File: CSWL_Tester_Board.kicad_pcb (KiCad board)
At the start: 2 copper layers, 164 parts, among them J1 DB9_Female ID09S33E4GV00LF, J10 Conn_01x03_Male, J11 Conn_01x02, J12 Conn_01x02, J13 Conn_01x02, J14 Conn_01x04, J15 SPI1, J16 Conn_02x10_Odd_Even, J17 Conn_01x02, J18 Conn_01x02, J19 Conn_01x02, J2 Conn_01x04, J20 Conn_01x02, J22 Conn_01x02, J23 Conn_01x03, J24 Conn_01x02, J25 USB_B_Micro, J26 Conn_01x04, J27 Conn_01x10, J3 Conn_01x04, J4 Conn_01x04, J5 DB9_Female ID09S33E4GV00LF, J6 Conn_01x04, J7 Conn_01x04, J8 DB9_Female ID09S33E4GV00LF, J9 Conn_Coaxial_Power, K1 G6SU-2 DC5, K2 G6SU-2 DC5, K3 G6SU-2 DC5, K4 G6SU-2 DC5, K5 G6SU-2 DC5, Q1 DMG2301L, Q10 2N7002LT1G, Q11 2N7002LT1G, Q2 DMG2301L, Q3 DMG2301L, Q4 2N7002LT1G, Q5 2N7002LT1G, Q6 2N7002LT1G, Q7 DMG2301L, Q8 DMG2301L, U1 MAX3221EIPW, U10 EL817-S1-A (NC), U2 STM32F103RCT6, U3 MAX3221EIPW, U4 MCP1700T-3302E_TT, U5 MAX3221EIPW, U6 EL817-S1-A (NC), U7 EL817-S1-A (NC), U8 EL817-S1-A (NC), U9 EL817-S1-A (NC), Y1 8MHz

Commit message: Ruan: pcb developing
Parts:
- removed R62, R68, R70, R71: 0R, Resistor_SMD:R_0603_1608Metric
- added J21: Fix hole, RuanProject:Local_Hole_D5.0mm_Drill3.5mm, F.Cu at (156.5, 127.0)
- added J28: Fix hole, RuanProject:Local_Hole_D5.0mm_Drill3.5mm, F.Cu at (41.1, 127.0)
- added J29: Fix hole, RuanProject:Local_Hole_D5.0mm_Drill3.5mm, F.Cu at (40.6, 40.1)
- added J30: Fix hole, RuanProject:Local_Hole_D5.0mm_Drill3.5mm, F.Cu at (156.0, 40.1)
- added J31: Conn_Coaxial_Power, Connector_BarrelJack:BarrelJack_Horizontal, F.Cu at (62.2, 123.3)
- moved TP4 167.7 mm to (158.6, 85.7), turned to 90 degrees
- moved TP1 165.7 mm to (153.8, 85.8), turned to 90 degrees
- moved TP2 163.9 mm to (158.6, 89.1), turned to 90 degrees
- moved TP3 156.6 mm to (153.7, 89.2), turned to 90 degrees
- moved R4 137.8 mm to (41.7, 60.1)
- moved R7 137.7 mm to (44.7, 60.2)
- moved J6 134.3 mm to (42.1, 55.4)
- moved J16 117.6 mm to (122.2, 88.9), turned to 90 degrees
- moved J23 114.1 mm to (113.0, 65.4), turned to 270 degrees
- moved J14 94.9 mm to (119.8, 66.2), turned to 90 degrees
- moved R33 92.3 mm to (120.9, 70.8), turned to 90 degrees
- moved R32 87.9 mm to (124.0, 70.8), turned to 90 degrees
- moved R38 84.6 mm to (150.0, 108.1)
- moved R40 84.6 mm to (156.2, 104.2)
- moved U6 84.6 mm to (147.6, 100.1)
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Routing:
- net GND: track 0.00 -> 443.4 mm
- net GNDS: track 0.00 -> 272.3 mm
- net +5V: track 0.00 -> 197.8 mm
- net +5VA: track 0.00 -> 160.7 mm, vias 0 -> 2
- net /Vuart: track 0.00 -> 122.6 mm, vias 0 -> 4
- net /CSWL-: track 0.00 -> 106.6 mm
- net /CSWL+: track 0.00 -> 91.0 mm
- net +3V3: track 0.00 -> 83.8 mm, vias 0 -> 1
- net /VMeter-: track 0.00 -> 61.9 mm
- net /VMeter+: track 0.00 -> 46.7 mm
- net /Resistor+: track 0.00 -> 32.9 mm
- net /Uart2_TX: track 0.00 -> 26.9 mm
- net /Uart3_TX: track 0.00 -> 26.5 mm
- net Net-(J1-Pad7): track 0.00 -> 26.3 mm, vias 0 -> 1
- net /Uart1_TX: track 0.00 -> 26.2 mm, vias 0 -> 1
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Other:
- board outline added: 125.5 x 98 mm

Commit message: Ruan: base ok V0
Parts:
- added R62: 100K, Resistor_SMD:R_0603_1608Metric, B.Cu at (45.0, 123.3)
- added R68: 0R, Resistor_SMD:R_0603_1608Metric, B.Cu at (134.4, 68.7)
- added R70: 0R, Resistor_SMD:R_0603_1608Metric, B.Cu at (145.2, 68.9)
- added R71: 0R, Resistor_SMD:R_0603_1608Metric, B.Cu at (151.1, 68.9)
- moved TP2 6.81 mm to (152.8, 85.6)
- moved TP4 6.64 mm to (152.8, 82.5)
- moved TP1 5.93 mm to (152.8, 91.7)
- moved J23 4.98 mm to (108.1, 65.9)
- moved R60 3.89 mm to (130.3, 106.8), turned to 90 degrees
- moved R31 3.06 mm to (124.0, 70.6)
- moved R32 3.06 mm to (120.9, 70.6)
- moved R33 3.06 mm to (117.9, 70.6)
- moved J27 3.00 mm to (154.8, 65.3)
- moved R63 2.80 mm to (127.2, 105.9), turned to 180 degrees
- moved J12 1.78 mm to (142.5, 72.3)
- moved R22 1.78 mm to (133.2, 76.2)
- moved R23 1.78 mm to (141.5, 76.2)
- moved R24 1.78 mm to (151.0, 76.2)
- moved J13 1.78 mm to (151.5, 72.4)
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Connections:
- J11 pad 1: GND -> GNDA1
- J12 pad 1: GND -> GNDA2
- J13 pad 1: GND -> GNDA3
- J16 pad 1: /CSWL+ -> /CSWL-
- J16 pad 11: /CSWL_IN- -> /CSWL_IN+
- J16 pad 13: /CSWL_IN+ -> /CSWL_IN-
- J16 pad 15: /CSWL_IN+ -> /CSWL_IN-
- J16 pad 17: /CSWL_VMeter+ -> /CSWL_VMeter-
- J16 pad 19: /CSWL_VMeter- -> /CSWL_VMeter+
- J16 pad 3: /CSWL+ -> /CSWL-
- J16 pad 5: /CSWL- -> /CSWL+
- J16 pad 7: /CSWL- -> /CSWL+
- J16 pad 9: /CSWL_IN- -> /CSWL_IN+
- J27 pad 1: /GPA8 -> /GPB1
- J27 pad 2: /GPB1 -> /GPB2
- J27 pad 3: /GPB2 -> /GPC1
- J27 pad 4: /GPB12 -> /GPC0
- J27 pad 5: /GPB13 -> /GPB12
- J27 pad 6: /GPB14 -> /GPB13
- J27 pad 7: /GPB15 -> /GPB14
- J27 pad 8: /GPC0 -> /GPB15
- J27 pad 9: /GPC1 -> /GPA8
- R22 pad 2: GND -> GNDA1
- R23 pad 2: GND -> GNDA2
- R24 pad 2: GND -> GNDA3
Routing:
- net +3V3: track 83.8 -> 487.1 mm, vias 1 -> 26
- net GND: track 443.4 -> 688.9 mm, vias 0 -> 81
- net +5VA: track 160.7 -> 312.9 mm, vias 2 -> 7
- net /Uart4_TX: track 15.2 -> 142.6 mm, vias 0 -> 2
- net /Uart4_RX: track 12.3 -> 139.3 mm, vias 0 -> 2
- net +5V: track 197.8 -> 279.8 mm
- net /GPA1: track 0.00 -> 80.0 mm, vias 0 -> 2
- net /GPB1: track 4.64 -> 83.4 mm, vias 0 -> 2
- net /GPB0: track 4.27 -> 81.3 mm, vias 0 -> 2
- net /GPC1: track 3.71 -> 80.2 mm, vias 0 -> 4
- net /Uart3_TX: track 26.5 -> 102.8 mm, vias 0 -> 2
- net /GPB2: track 4.76 -> 80.7 mm, vias 0 -> 2
- net /Power_EN: track 9.46 -> 84.7 mm, vias 0 -> 4
- net /GPC0: track 3.31 -> 77.1 mm, vias 0 -> 4
- net /Uart3_RX: track 22.0 -> 92.3 mm, vias 1 -> 3
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- added copper zone on B.Cu, net GND
- added copper zone on F.Cu, net GND
- added copper zone on F.Cu, net GNDA
- added copper zone on B.Cu, net GNDA1
- added copper zone on B.Cu, net GNDA2
- added copper zone on B.Cu, net GNDA3
- added copper zone on F.Cu, net GNDS
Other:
- board text added: "5V"
- board text added: "A0"
- board text added: "A1"
- board text added: "A8"
- board text added: "B0"
- board text added: "B1"
- board text added: "B12"
- board text added: "B13"
- board text added: "B14"
- board text added: "B15"
- board text added: "B2"
- board text added: "C0"
- board text added: "C1"
- board text added: "CLK"
- board text added: "CS_IN+"
- board text added: "CS_IN-"
- board text added: "CS_OUT-"
- board text added: "CS_Out+"
- board text added: "DIO"
- board text added: "G"
- board text added: "Gnd"
- board text added: "Int"
- board text added: "MI"
- board text added: "MO"
- board text added: "NSS"
- board text added: "R"
- board text added: "Rload+"
- board text added: "Rload-"
- board text added: "Rx"
- board text added: "SCK"
- board text added: "SCL"
- board text added: "SDA"
- board text added: "Shave+"
- board text added: "Shave-"
- board text added: "T"
- board text added: "Tx"
- board text added: "Uart1"
- board text added: "Uart4"
- board text added: "Uart5"
- board text added: "Usart2"
- board text added: "Usart3"
- board text added: "VMeter+"
- board text added: "VMeter-"
- board text added: "Vmeter+"
- board text added: "Vmeter-"

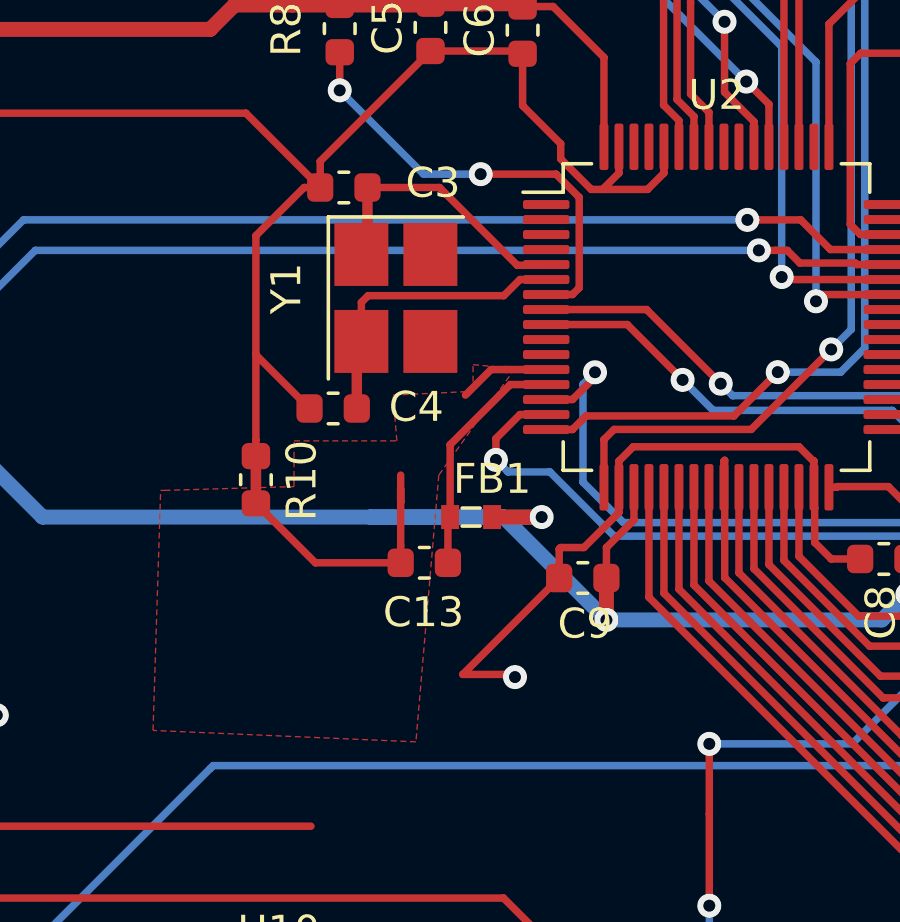
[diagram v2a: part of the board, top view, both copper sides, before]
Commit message: Ruan: improve the crystal path
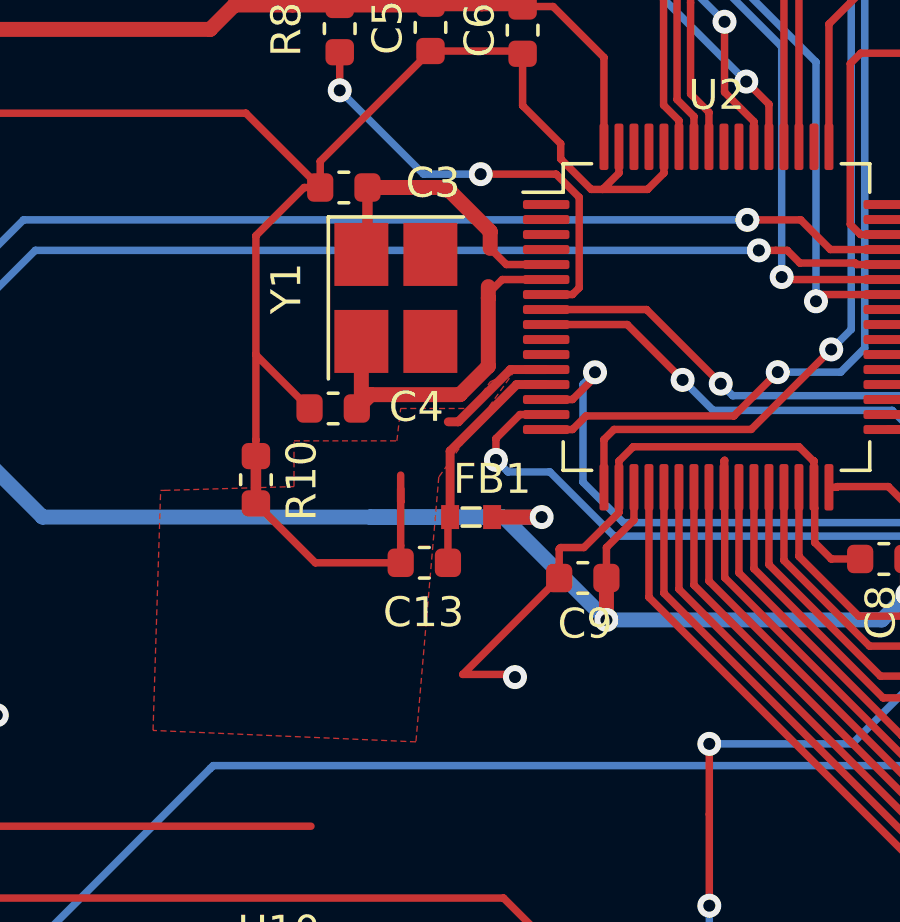
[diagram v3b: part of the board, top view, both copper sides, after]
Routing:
- net Net-(C4-Pad2): track 10.1 -> 12.2 mm
- net GNDA: track 12.0 -> 13.0 mm
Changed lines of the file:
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@@
     (thickness 1.6)
     (drawings 72)
-    (tracks 2026)
+    (tracks 2030)
     (zones 0)
     (modules 169)
@@
   (segment (start 74.33076 73.5919) (end 74.12736 73.7953) (width 0.35) (layer F.Cu) (net 5))
   (segment (start 74.33076 71.5645) (end 74.33076 73.5919) (width 0.35) (layer F.Cu) (net 5))
-  (segment (start 80.26377 74.15749) (end 80.28876 74.1325) (width 0.25) (layer F.Cu) (net 5))
-  (segment (start 79.324552 74.15749) (end 80.26377 74.15749) (width 0.25) (layer F.Cu) (net 5))
-  (segment (start 74.33076 71.5645) (end 76.731562 71.5645) (width 0.25) (layer F.Cu) (net 5))
-  (segment (start 76.731562 71.5645) (end 79.324552 74.15749) (width 0.25) (layer F.Cu) (net 5))
+  (segment (start 76.956562 71.5645) (end 78.4225 73.030438) (width 0.5) (layer F.Cu) (net 5))
+  (segment (start 74.33076 71.5645) (end 76.956562 71.5645) (width 0.5) (layer F.Cu) (net 5))
+  (segment (start 78.4225 73.030438) (end 78.4225 73.5965) (width 0.5) (layer F.Cu) (net 5))
+  (segment (start 78.9585 74.1325) (end 78.4225 73.5965) (width 0.25) (layer F.Cu) (net 5))
+  (segment (start 80.28876 74.1325) (end 78.9585 74.1325) (width 0.25) (layer F.Cu) (net 5))
   (segment (start 53.56362 46.99488) (end 53.594 46.9645) (width 0.35) (layer F.Cu) (net 6))
   (segment (start 51.77282 46.99488) (end 53.56362 46.99488) (width 0.35) (layer F.Cu) (net 6))
@@
   (segment (start 131.953 66.929) (end 132.969 67.945) (width 0.25) (layer B.Cu) (net 6))
   (segment (start 39.624 101.549) (end 39.624 100.203) (width 0.5) (layer F.Cu) (net 6))
-  (segment (start 73.97516 76.8475) (end 74.12736 76.6953) (width 0.35) (layer F.Cu) (net 7))
-  (segment (start 73.97516 78.9305) (end 73.97516 76.8475) (width 0.35) (layer F.Cu) (net 7))
-  (segment (start 79.41376 74.6325) (end 80.28876 74.6325) (width 0.25) (layer F.Cu) (net 7))
-  (segment (start 78.875959 75.170301) (end 79.41376 74.6325) (width 0.25) (layer F.Cu) (net 7))
-  (segment (start 74.352359 75.170301) (end 78.875959 75.170301) (width 0.25) (layer F.Cu) (net 7))
-  (segment (start 74.12736 75.3953) (end 74.352359 75.170301) (width 0.25) (layer F.Cu) (net 7))
-  (segment (start 74.12736 76.6953) (end 74.12736 75.3953) (width 0.25) (layer F.Cu) (net 7))
+  (segment (start 77.413774 78.468888) (end 78.359 77.523662) (width 0.5) (layer F.Cu) (net 7))
+  (segment (start 73.97516 78.9305) (end 74.436772 78.468888) (width 0.5) (layer F.Cu) (net 7))
+  (segment (start 74.436772 78.468888) (end 77.413774 78.468888) (width 0.5) (layer F.Cu) (net 7))
+  (segment (start 78.359 75.09559) (end 78.359 75.2475) (width 0.25) (layer F.Cu) (net 7))
+  (segment (start 78.82209 74.6325) (end 78.359 75.09559) (width 0.25) (layer F.Cu) (net 7))
+  (segment (start 80.28876 74.6325) (end 78.82209 74.6325) (width 0.25) (layer F.Cu) (net 7))
+  (segment (start 78.359 77.523662) (end 78.359 75.2475) (width 0.5) (layer F.Cu) (net 7))
+  (segment (start 78.359 75.2475) (end 78.359 74.8665) (width 0.5) (layer F.Cu) (net 7))
+  (segment (start 74.12736 78.7783) (end 73.97516 78.9305) (width 0.5) (layer F.Cu) (net 7))
+  (segment (start 74.12736 76.6953) (end 74.12736 78.7783) (width 0.5) (layer F.Cu) (net 7))
   (segment (start 61.214 63.326) (end 60.024 64.516) (width 0.5) (layer B.Cu) (net 8))
   (segment (start 61.214 61.976) (end 61.214 63.326) (width 0.5) (layer B.Cu) (net 8))
@@
   (segment (start 75.438 83.499) (end 75.438 84.074) (width 0.25) (layer F.Cu) (net 12))
   (segment (start 75.438 81.15159) (end 75.438 82.042) (width 0.25) (layer F.Cu) (net 12))
-  (segment (start 80.28876 77.6325) (end 78.95709 77.6325) (width 0.25) (layer F.Cu) (net 12))
   (segment (start 75.438 81.60826) (end 75.438 82.042) (width 0.25) (layer F.Cu) (net 12))
   (segment (start 75.438 82.042) (end 75.438 83.499) (width 0.25) (layer F.Cu) (net 12))
   (segment (start 72.593 84.074) (end 75.438 84.074) (width 0.25) (layer F.Cu) (net 12))
   (segment (start 70.612 82.093) (end 72.593 84.074) (width 0.25) (layer F.Cu) (net 12))
-  (segment (start 78.95709 77.6325) (end 78.4505 77.6325) (width 0.25) (layer F.Cu) (net 12))
-  (segment (start 78.4505 77.6325) (end 77.597 78.486) (width 0.25) (layer F.Cu) (net 12))
-  (segment (start 80.28876 78.1325) (end 79.0935 78.1325) (width 0.25) (layer F.Cu) (net 13))
-  (segment (start 77.086 80.14) (end 77.086 82.55) (width 0.25) (layer F.Cu) (net 13))
-  (segment (start 79.0935 78.1325) (end 77.086 80.14) (width 0.25) (layer F.Cu) (net 13))
+  (segment (start 79.098704 77.6325) (end 77.356204 79.375) (width 0.3) (layer F.Cu) (net 12))
+  (segment (start 80.28876 77.6325) (end 79.098704 77.6325) (width 0.3) (layer F.Cu) (net 12))
+  (segment (start 77.356204 79.375) (end 77.0255 79.375) (width 0.3) (layer F.Cu) (net 12))
   (segment (start 77.013 82.623) (end 77.086 82.55) (width 0.25) (layer F.Cu) (net 13))
   (segment (start 77.013 84.074) (end 77.013 82.623) (width 0.25) (layer F.Cu) (net 13))
+  (segment (start 80.28876 78.1325) (end 79.305824 78.1325) (width 0.3) (layer F.Cu) (net 13))
+  (segment (start 77.086 80.352324) (end 77.086 82.55) (width 0.3) (layer F.Cu) (net 13))
+  (segment (start 79.305824 78.1325) (end 77.086 80.352324) (width 0.3) (layer F.Cu) (net 13))
   (segment (start 123.40814 52.04726) (end 124.40814 52.04726) (width 0.25) (layer F.Cu) (net 14))
   (segment (start 121.666 51.562) (end 122.92288 51.562) (width 0.25) (layer F.Cu) (net 14))
@@
     )
   )
-  (zone (net 12) (net_name GNDA) (layer F.Cu) (hatch edge 0.508)
-    (connect_pads (clearance 0.508))
-    (min_thickness 0.254)
-    (fill yes (arc_segments 32) (thermal_gap 0.508) (thermal_bridge_width 0.508))
-    (polygon
-      (pts
-        (xy 67.564 81.661) (xy 71.882 81.534) (xy 71.882 80.01) (xy 75.311 80.01) (xy 75.184 78.486)
-        (xy 77.851 78.359) (xy 77.851 77.47) (xy 79.248 77.597) (xy 76.708 81.153) (xy 75.946 90.043)
-        (xy 67.183 89.662) (xy 67.437 81.661)
-      )
-    )
-  )
   (zone (net 0) (net_name "") (layer F.Cu) (hatch edge 0.508)
     (connect_pads (clearance 0.508))
@@
       )
     )
+  )
+  (zone (net 12) (net_name GNDA) (layer F.Cu) (hatch edge 0.508)
+    (connect_pads (clearance 0.508))
+    (min_thickness 0.254)
+    (fill yes (arc_segments 32) (thermal_gap 0.508) (thermal_bridge_width 0.508))
+    (polygon
+      (pts
+        (xy 67.564 81.661) (xy 71.882 81.534) (xy 71.882 80.01) (xy 75.311 80.01) (xy 75.438 78.9305)
+        (xy 77.7875 78.9305) (xy 78.4225 78.0415) (xy 79.248 77.6605) (xy 76.708 81.2165) (xy 75.946 90.043)
+        (xy 67.183 89.662) (xy 67.437 81.661)
+      )
+    )

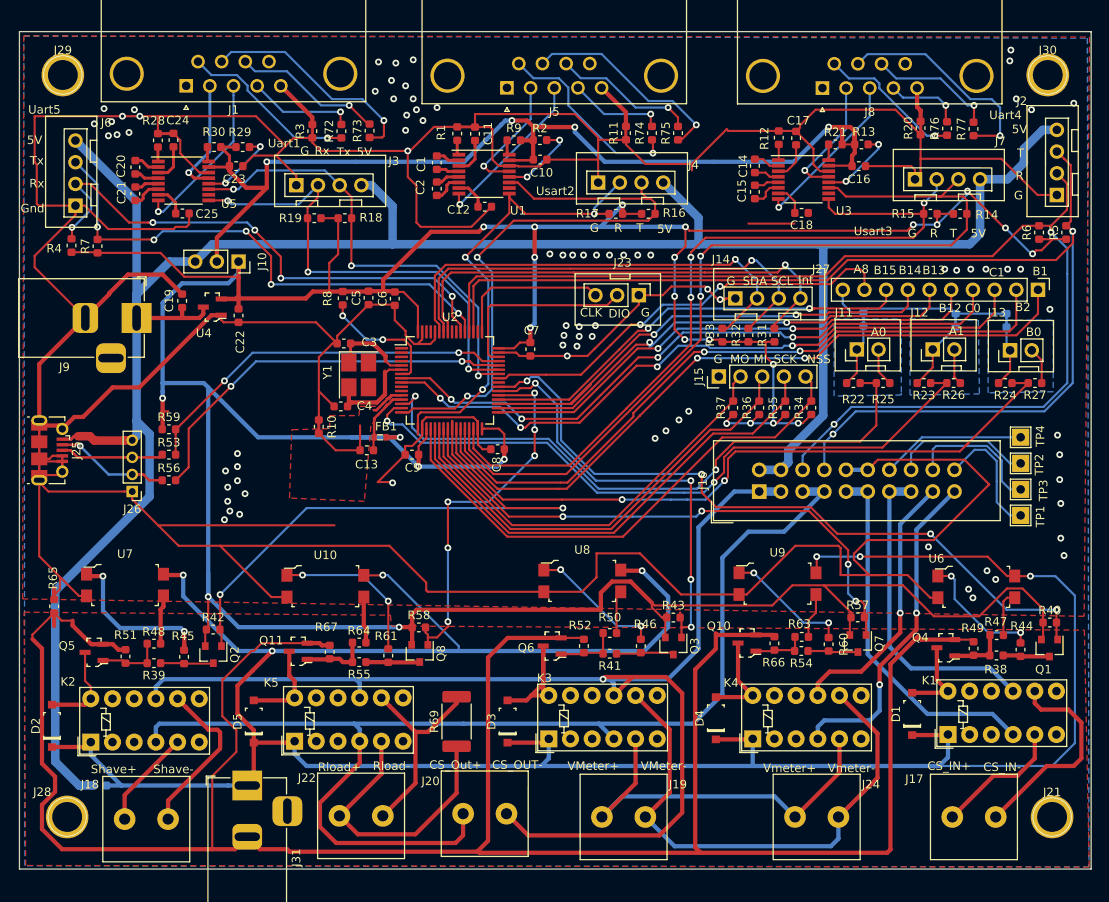
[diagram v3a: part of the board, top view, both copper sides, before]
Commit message: Ruan: add more function on ADC connector
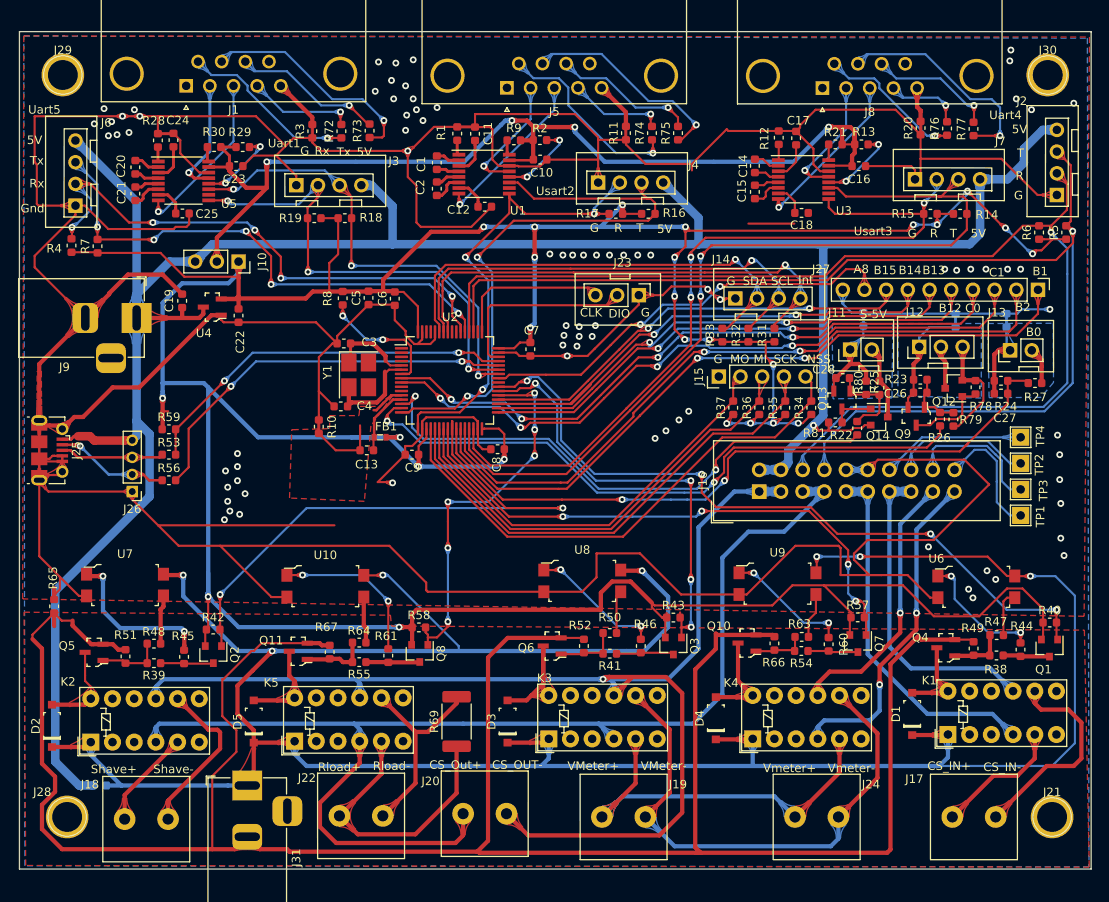
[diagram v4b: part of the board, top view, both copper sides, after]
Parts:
- added C26: 0.1uF, Capacitor_SMD:C_0603_1608Metric, F.Cu at (141.0, 77.3)
- added C27: 0.1uF, Capacitor_SMD:C_0603_1608Metric, F.Cu at (150.5, 77.4)
- added C28: 0.1uF, Capacitor_SMD:C_0603_1608Metric, F.Cu at (132.0, 75.6)
- added Q12: DMG2301L, Package_TO_SOT_SMD:SOT-23, F.Cu at (144.9, 76.8)
- added Q13: 2N7002LT1G, digikey-footprints:SOT-23-3, F.Cu at (131.9, 78.2)
- added Q14: DMG2301L, Package_TO_SOT_SMD:SOT-23, F.Cu at (136.2, 80.2)
- added Q9: 2N7002LT1G, digikey-footprints:SOT-23-3, F.Cu at (140.6, 80.1)
- added R78: 100K, Resistor_SMD:R_0603_1608Metric, F.Cu at (147.5, 76.7)
- added R79: 0R ( NC ), Resistor_SMD:R_0603_1608Metric, F.Cu at (144.9, 80.5)
- added R80: 100K, Resistor_SMD:R_0603_1608Metric, F.Cu at (134.7, 76.8)
- added R81: 100K, Resistor_SMD:R_0603_1608Metric, F.Cu at (131.1, 80.8)
- J12: value Conn_01x02 -> Conn_01x03; footprint RuanProject:Connector_Set_1x02_P2.54mm_Vertical -> RuanProject:Connector_Set_1x03_P2.54mm_Vertical
- R22: value 10K -> 33R
- R23: value 10K -> 100K
- R26: value 0R -> 33R
- R27: value 0R -> 1K
- moved R22 5.30 mm to (133.6, 81.5), turned to 90 degrees
- moved R26 4.52 mm to (143.3, 80.4), turned to 90 degrees
- moved J12 1.61 mm to (140.9, 72.0)
- moved J11 0.79 mm to (132.8, 72.3)
- moved R25 0.71 mm to (136.2, 76.8), turned to 270 degrees
- moved R23 0.58 mm to (141.0, 75.8)
- moved R24 0.56 mm to (150.5, 75.9)
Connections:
- R22 pad 2: GNDA1 -> Net-(C28-Pad2)
- R23 pad 1: /GPA1 -> Net-(C26-Pad2)
- R25 pad 1: /GPA0 -> Net-(J11-Pad2)
- R25 pad 2: Net-(J11-Pad2) -> Net-(C28-Pad2)
- R26 pad 2: Net-(J12-Pad2) -> Net-(C26-Pad2)
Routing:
- net Net-(J12-Pad3): track 0.00 -> 13.3 mm
- net Net-(C28-Pad2): track 0.00 -> 10.6 mm
- net Net-(Q12-Pad1): track 0.00 -> 9.71 mm
- net /GPA0: track 73.9 -> 64.3 mm
- net +5V: track 279.8 -> 288.0 mm, vias 0 -> 1
- net Net-(C26-Pad2): track 0.00 -> 7.02 mm
- net GNDA2: track 8.45 -> 13.5 mm
- net Net-(Q13-Pad3): track 0.00 -> 4.96 mm
- net GNDA1: track 7.49 -> 12.4 mm
- net GND: track 688.9 -> 693.8 mm
- net /GPA1: track 80.0 -> 75.8 mm
- net Net-(J11-Pad2): track 4.48 -> 8.67 mm
- net GNDA3: track 7.28 -> 9.51 mm
- net Net-(J12-Pad2): track 4.22 -> 5.07 mm
- net /Uart4_TX: vias 2 -> 1
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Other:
- board text added: "In"
- board text added: "Out"
- board text added: "S-5V"
- board text removed: "A0"
- board text removed: "A1"
